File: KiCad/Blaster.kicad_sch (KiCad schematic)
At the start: 32 parts, among them Q1 2N3904, Q2 2N3904, Q3 TIP41, SW2 Fire, SW3 Freq Select, SW4 Fire Select, U2 PIC16F1788-IP, U3 Audio Board

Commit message: Updated blaster schematic
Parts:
- R13: value 40kΩ -> 25kΩ
- R6: value 1kΩ -> 2.2kΩ
- renumbered D5 to D4, D6 to D5
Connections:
- net +5V: no longer D5.1 (K), Q2.3 (C), S1. (-)
- new net: D5.1 (K), Q2.3 (C), S1. (-)
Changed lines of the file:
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@@
 	)
 	(junction
+		(at 237.49 100.33)
+		(diameter 0)
+		(color 0 0 0 0)
+	)
+	(junction
 		(at 33.02 77.47)
 		(diameter 0)
@@
 	)
 	(junction
-		(at 237.49 100.33)
-		(diameter 0)
-		(color 0 0 0 0)
-	)
-	(junction
 		(at 224.79 100.33)
 		(diameter 0)
@@
 	(wire
 		(pts
+			(xy 237.49 99.06) (xy 237.49 100.33)
+		)
+		(stroke
+			(width 0)
+			(type default)
+		)
+	)
+	(wire
+		(pts
 			(xy 57.15 101.6) (xy 52.07 101.6)
 		)
@@
 		(dnp no)
 		(property "Reference" "R13"
-			(at 199.39 113.03 0)
+			(at 199.898 113.03 0)
 			(effects
 				(font
@@
 			)
 		)
-		(property "Value" "40kΩ"
+		(property "Value" "25kΩ"
 			(at 200.914 115.57 0)
 			(effects
@@
 		(dnp no)
 		(fields_autoplaced yes)
-		(property "Reference" "#PWR011"
+		(property "Reference" "#PWR013"
 			(at 81.28 59.69 90)
 			(effects
@@
 			(project "Project"
 				(path "/152b0fc1-fa29-4f64-bd5c-6a59f63b05cf/0b035578-8811-407f-9c52-5736444552f1"
-					(reference "#PWR011")
+					(reference "#PWR013")
 					(unit 1)
 				)
@@
 		(dnp no)
 		(fields_autoplaced yes)
-		(property "Reference" "#PWR010"
+		(property "Reference" "#PWR012"
 			(at 113.03 55.88 90)
 			(effects
@@
 			(project "Project"
 				(path "/152b0fc1-fa29-4f64-bd5c-6a59f63b05cf/0b035578-8811-407f-9c52-5736444552f1"
-					(reference "#PWR010")
+					(reference "#PWR012")
 					(unit 1)
 				)
@@
 		(dnp no)
 		(fields_autoplaced yes)
-		(property "Reference" "#PWR014"
+		(property "Reference" "#PWR016"
 			(at 124.46 115.57 90)
 			(effects
@@
 			(project "Project"
 				(path "/152b0fc1-fa29-4f64-bd5c-6a59f63b05cf/0b035578-8811-407f-9c52-5736444552f1"
-					(reference "#PWR014")
+					(reference "#PWR016")
 					(unit 1)
 				)
@@
 		(dnp no)
 		(fields_autoplaced yes)
-		(property "Reference" "#PWR09"
+		(property "Reference" "#PWR011"
 			(at 52.07 55.88 90)
 			(effects
@@
 			(project "Project"
 				(path "/152b0fc1-fa29-4f64-bd5c-6a59f63b05cf/0b035578-8811-407f-9c52-5736444552f1"
-					(reference "#PWR09")
+					(reference "#PWR011")
 					(unit 1)
 				)
@@
 		(dnp no)
 		(fields_autoplaced yes)
-		(property "Reference" "#PWR016"
+		(property "Reference" "#PWR018"
 			(at 83.82 185.42 90)
 			(effects
@@
 			(project "Project"
 				(path "/152b0fc1-fa29-4f64-bd5c-6a59f63b05cf/0b035578-8811-407f-9c52-5736444552f1"
-					(reference "#PWR016")
+					(reference "#PWR018")
 					(unit 1)
 				)
@@
 		(on_board yes)
 		(dnp no)
-		(property "Reference" "D6"
+		(property "Reference" "D5"
 			(at 226.568 104.394 90)
 			(effects
@@
 			(project "Project"
 				(path "/152b0fc1-fa29-4f64-bd5c-6a59f63b05cf/0b035578-8811-407f-9c52-5736444552f1"
-					(reference "D6")
+					(reference "D5")
 					(unit 1)
 				)
@@
 	)
 	(symbol
-		(lib_id "Libraries:+5V")
-		(at 237.49 99.06 0)
+		(lib_id "AW_Libraries_Power:GND")
+		(at 85.09 102.87 0)
 		(unit 1)
 		(exclude_from_sim no)
@@
 		(dnp no)
 		(fields_autoplaced yes)
-		(property "Reference" "+5V07"
-			(at 237.49 95.25 0)
+		(property "Reference" "#PWR015"
+			(at 81.28 102.87 90)
 			(effects
 				(font
@@
 			)
 		)
-		(property "Value" "+5V"
-			(at 237.49 95.25 0)
+		(property "Value" "GND"
+			(at 81.28 99.06 0)
 			(effects
 				(font
@@
 		)
 		(property "Footprint" ""
-			(at 237.49 95.25 0)
+			(at 85.09 102.87 0)
 			(effects
 				(font
@@
 		)
 		(property "Datasheet" ""
-			(at 237.49 95.25 0)
+			(at 85.09 102.87 0)
 			(effects
 				(font
@@
 		)
 		(property "Description" ""
-			(at 237.49 99.06 0)
+			(at 85.09 102.87 0)
 			(effects
 				(font
@@
 			(project "Project"
 				(path "/152b0fc1-fa29-4f64-bd5c-6a59f63b05cf/0b035578-8811-407f-9c52-5736444552f1"
-					(reference "+5V07")
+					(reference "#PWR015")
 					(unit 1)
 				)
@@
 	)
 	(symbol
-		(lib_id "AW_Libraries_Power:GND")
-		(at 85.09 102.87 0)
+		(lib_id "Libraries:Solenoid")
+		(at 237.49 97.79 0)
 		(unit 1)
 		(exclude_from_sim no)
-		(in_bom no)
-		(on_board no)
+		(in_bom yes)
+		(on_board yes)
 		(dnp no)
 		(fields_autoplaced yes)
-		(property "Reference" "#PWR013"
-			(at 81.28 102.87 90)
+		(property "Reference" "S1"
+			(at 250.19 107.9499 0)
 			(effects
 				(font
 					(size 1.27 1.27)
 				)
-				(hide yes)
+				(justify left)
 			)
 		)
-		(property "Value" "GND"
-			(at 81.28 99.06 0)
+		(property "Value" "Solenoid"
+			(at 250.19 110.4899 0)
 			(effects
 				(font
 					(size 1.27 1.27)
 				)
-				(hide yes)
+				(justify left)
 			)
 		)
-		(property "Footprint" ""
-			(at 85.09 102.87 0)
+		(property "Footprint" "Connector_PinHeader_2.54mm:PinHeader_1x02_P2.54mm_Vertical"
+			(at 239.776 102.87 0)
 			(effects
 				(font
@@
 		)
 		(property "Datasheet" ""
-			(at 85.09 102.87 0)
+			(at 239.776 102.87 0)
 			(effects
 				(font
@@
 		)
 		(property "Description" ""
-			(at 85.09 102.87 0)
+			(at 239.776 102.87 0)
 			(effects
 				(font
@@
 		(pin ""
 		)
+		(pin ""
+		)
 		(instances
 			(project "Project"
 				(path "/152b0fc1-fa29-4f64-bd5c-6a59f63b05cf/0b035578-8811-407f-9c52-5736444552f1"
-					(reference "#PWR013")
+					(reference "S1")
 					(unit 1)
 				)
@@
 	)
 	(symbol
-		(lib_id "Libraries:Solenoid")
-		(at 237.49 97.79 0)
+		(lib_id "Connector:TestPoint")
+		(at 190.5 81.28 0)
 		(unit 1)
 		(exclude_from_sim no)
@@
 		(on_board yes)
 		(dnp no)
-		(fields_autoplaced yes)
-		(property "Reference" "S1"
-			(at 250.19 107.9499 0)
+		(property "Reference" "TP6"
+			(at 188.722 75.692 0)
 			(effects
 				(font
@@
 			)
 		)
-		(property "Value" "Solenoid"
-			(at 250.19 110.4899 0)
+		(property "Value" "TestPoint"
+			(at 193.04 79.2479 0)
 			(effects
 				(font
@@
 				)
 				(justify left)
+				(hide yes)
 			)
 		)
-		(property "Footprint" "Connector_PinHeader_2.54mm:PinHeader_1x02_P2.54mm_Vertical"
-			(at 239.776 102.87 0)
+		(property "Footprint" "AlexWheelockFootprintLibrary:Test Point"
+			(at 195.58 81.28 0)
 			(effects
 				(font
@@
 			)
 		)
-		(property "Datasheet" ""
-			(at 239.776 102.87 0)
+		(property "Datasheet" "~"
+			(at 195.58 81.28 0)
 			(effects
 				(font
@@
 			)
 		)
-		(property "Description" ""
-			(at 239.776 102.87 0)
+		(property "Description" "test point"
+			(at 190.5 81.28 0)
 			(effects
 				(font
@@
 			)
 		)
-		(pin ""
-		)
-		(pin ""
+		(pin "1"
 		)
 		(instances
 			(project "Project"
 				(path "/152b0fc1-fa29-4f64-bd5c-6a59f63b05cf/0b035578-8811-407f-9c52-5736444552f1"
-					(reference "S1")
+					(reference "TP6")
 					(unit 1)
 				)
@@
 	)
 	(symbol
-		(lib_id "Connector:TestPoint")
-		(at 190.5 81.28 0)
+		(lib_id "AW_Libraries_Power:+7.4V")
+		(at 237.49 93.98 0)
 		(unit 1)
 		(exclude_from_sim no)
@@
 		(on_board yes)
 		(dnp no)
-		(property "Reference" "TP6"
-			(at 188.722 75.692 0)
+		(property "Reference" "#PWR19"
+			(at 237.49 93.98 0)
 			(effects
 				(font
 					(size 1.27 1.27)
 				)
-				(justify left)
+				(hide yes)
 			)
 		)
-		(property "Value" "TestPoint"
-			(at 193.04 79.2479 0)
+		(property "Value" "+7.4V"
+			(at 237.49 93.98 0)
 			(effects
 				(font
 					(size 1.27 1.27)
 				)
-				(justify left)
-				(hide yes)
 			)
 		)
-		(property "Footprint" "AlexWheelockFootprintLibrary:Test Point"
-			(at 195.58 81.28 0)
+		(property "Footprint" ""
+			(at 237.49 93.98 0)
 			(effects
 				(font
@@
 			)
 		)
-		(property "Datasheet" "~"
-			(at 195.58 81.28 0)
+		(property "Datasheet" ""
+			(at 237.49 93.98 0)
 			(effects
 				(font
@@
 			)
 		)
-		(property "Description" "test point"
-			(at 190.5 81.28 0)
+		(property "Description" ""
+			(at 237.49 93.98 0)
 			(effects
 				(font
@@
 			)
 		)
-		(pin "1"
+		(pin ""
 		)
 		(instances
 			(project "Project"
 				(path "/152b0fc1-fa29-4f64-bd5c-6a59f63b05cf/0b035578-8811-407f-9c52-5736444552f1"
-					(reference "TP6")
+					(reference "#PWR19")
 					(unit 1)
 				)
@@
 		(dnp no)
 		(fields_autoplaced yes)
-		(property "Reference" "#PWR015"
+		(property "Reference" "#PWR017"
 			(at 220.98 130.81 90)
 			(effects
@@
 			(project "Project"
 				(path "/152b0fc1-fa29-4f64-bd5c-6a59f63b05cf/0b035578-8811-407f-9c52-5736444552f1"
-					(reference "#PWR015")
+					(reference "#PWR017")
 					(unit 1)
 				)
@@
 			)
 		)
-		(property "Value" "1kΩ"
+		(property "Value" "2.2kΩ"
 			(at 199.898 78.74 0)
 			(effects
@@
 		(dnp no)
 		(fields_autoplaced yes)
-		(property "Reference" "#PWR012"
+		(property "Reference" "#PWR014"
 			(at 208.28 87.63 90)
 			(effects
@@
 			(project "Project"
 				(path "/152b0fc1-fa29-4f64-bd5c-6a59f63b05cf/0b035578-8811-407f-9c52-5736444552f1"
-					(reference "#PWR012")
+					(reference "#PWR014")
 					(unit 1)
 				)
@@
 		(dnp no)
 		(fields_autoplaced yes)
-		(property "Reference" "D5"
+		(property "Reference" "D4"
 			(at 83.82 45.72 0)
 			(effects
@@
 			(project "Project"
 				(path "/152b0fc1-fa29-4f64-bd5c-6a59f63b05cf/0b035578-8811-407f-9c52-5736444552f1"
-					(reference "D5")
+					(reference "D4")
 					(unit 1)
 				)

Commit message: Finalized schematics
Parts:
- removed Q1, Q2: 2N3904, Package_TO_SOT_THT:TO-92_Inline, symbol Transistor_BJT:2N3904
- removed Q3: TIP41, Package_TO_SOT_THT:TO-220-3_Vertical, symbol Transistor_BJT:TIP41
- removed SW3: Freq Select, symbol Switch:SW_DIP_x01
- removed TP1, TP2, TP3, TP4, TP5, TP6, TP7: TestPoint, AlexWheelockFootprintLibrary:Test Point, symbol Connector:TestPoint
- added Q1, Q2: BUK9832-55A, Package_TO_SOT_SMD:SOT-223-3_TabPin2, symbol Transistor_FET:BUK7880-55A
- added R15, R7: 0Ω, Resistor_SMD:R_0805_2012Metric_Pad1.20x1.40mm_HandSolder, symbol Libraries:R_Custom
- added SW3: Freq Select, AlexWheelockFootprintLibrary:Project_Blaster_Freq_Switch, symbol Switch:SW_SPDT
- D5: footprint (none) -> Diode_SMD:D_0805_2012Metric_Pad1.15x1.40mm_HandSolder
- LD1, S1: footprint Connector_PinHeader_2.54mm:PinHeader_1x02_P2.54mm_Vertical -> AlexWheelockFootprintLibrary:Project_Locking_Output_Header
- R14: renamed from R13; value 25kΩ -> 100kΩ
- R6: value 2.2kΩ -> 100kΩ
- SW2: footprint (none) -> AlexWheelockFootprintLibrary:Project_Locking_Output_Header
- SW4: footprint (none) -> AlexWheelockFootprintLibrary:Project_Blaster_FireSelect_Switch
- U2: footprint (none) -> AlexWheelockFootprintLibrary:SSOP-28
- U3: footprint (none) -> AlexWheelockFootprintLibrary:Project_Audio_Board
- renumbered R9 to R10, R10 to R11, R11 to R12, R12 to R13, R7 to R8, R8 to R9
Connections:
- net +5V: now also SW3.2 (B)
- net at R14.1: now also U2.14 (RC3/SCK/SCL), Q2.1 (G)
- net at R14.2: no longer U2.14 (RC3/SCK/SCL)
- net at LD1.3 (K): now also Q1.2 (D)
- net at D5.1 (K): now also S1.1 (+); no longer S1. (-)
- net at R6.1: now also U2.13 (RC2/P1A/CCP1), Q1.1 (G)
- net at R13.1: now also S1.2 (-), Q2.2 (D); no longer S1. (-)
- net at R6.2: no longer U2.13 (RC2/P1A/CCP1)
- new net: Q1.3 (S), R7.1
- new net: C8.2, R8.1, SW2.2, U2.21 (INT/AN12/RB0)
- new net: R10.1, SW4.5, U2.23 (P1B/AN8/RB2)
- new net: R9.1, SW3.1 (A), U2.22 (P1C/AN10/RB1)
- new net: Q2.3 (S), R15.1
- no-connect marks 15 -> 16
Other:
- note added: "R8-R12 330Ω"
- note removed: "R7-R11 330Ω"
- moved on the sheet: D5, LD1, R13, R14, R6

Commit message: working on the PCB for the blaster
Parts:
- SW4: footprint AlexWheelockFootprintLibrary:Project_Blaster_FireSelect_Switch -> AlexWheelockFootprintLibrary:Project_Locking_Header_1x06
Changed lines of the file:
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@@
 			)
 		)
-		(property "Footprint" "AlexWheelockFootprintLibrary:Project_Blaster_FireSelect_Switch"
+		(property "Footprint" "AlexWheelockFootprintLibrary:Project_Locking_Header_1x06"
 			(at 44.45 96.52 0)
 			(effects

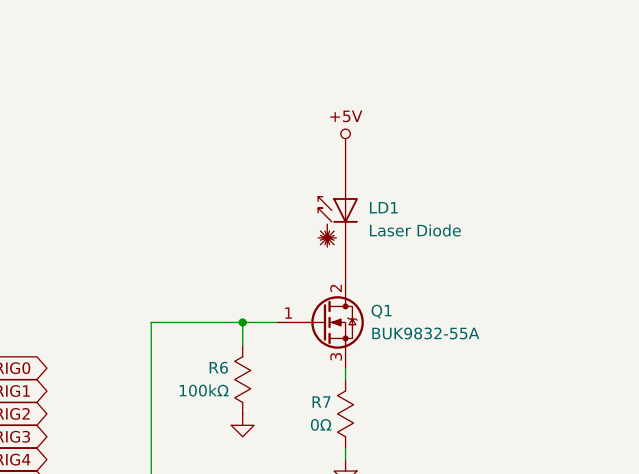
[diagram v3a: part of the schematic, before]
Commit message: got a lot done on the blaster PCB
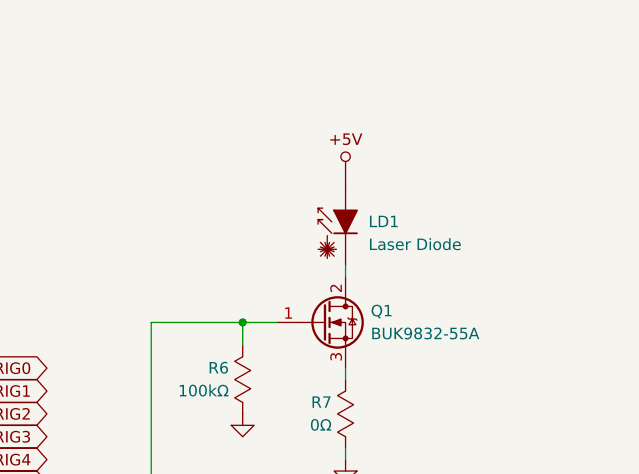
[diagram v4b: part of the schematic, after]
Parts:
- LD1: symbol Device:D_Laser_1A3C -> Libraries:Laser_Diode
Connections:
- net at Q1.2 (D): now also LD1.2 (K); no longer LD1.3 (K)
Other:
- moved on the sheet: LD1
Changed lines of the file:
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@@
 	(wire
 		(pts
+			(xy 205.74 53.34) (xy 205.74 54.61)
+		)
+		(stroke
+			(width 0)
+			(type default)
+		)
+	)
+	(wire
+		(pts
 			(xy 198.12 100.33) (xy 198.12 102.87)
 		)
@@
 	)
 	(symbol
-		(lib_id "Device:D_Laser_1A3C")
-		(at 205.74 46.99 90)
+		(lib_id "Libraries:Laser_Diode")
+		(at 198.12 48.26 90)
 		(unit 1)
 		(exclude_from_sim no)
@@
 		(fields_autoplaced yes)
 		(property "Reference" "LD1"
-			(at 208.28 46.9899 90)
+			(at 208.28 48.5139 90)
 			(effects
 				(font
@@
 		)
 		(property "Value" "Laser Diode"
-			(at 208.28 49.5299 90)
+			(at 208.28 51.0539 90)
 			(effects
 				(font
@@
 		)
 		(property "Footprint" "AlexWheelockFootprintLibrary:Project_Locking_Output_Header"
-			(at 206.375 49.53 0)
+			(at 198.12 48.26 0)
 			(effects
 				(font
@@
 		)
 		(property "Datasheet" "~"
-			(at 210.82 46.228 0)
+			(at 198.12 48.26 0)
 			(effects
 				(font
@@
 		)
 		(property "Description" "Laser diode, cathode on pin 3, anode on pin 1"
-			(at 205.74 46.99 0)
+			(at 198.12 48.26 0)
 			(effects
 				(font
@@
 		(pin "1"
 		)
-		(pin "3"
+		(pin "2"
 		)
 		(instances
@@
 	(symbol
 		(lib_id "Libraries:+5V")
-		(at 205.74 40.64 0)
+		(at 205.74 43.18 0)
 		(unit 1)
 		(exclude_from_sim no)
@@
 		(fields_autoplaced yes)
 		(property "Reference" "#+5V03"
-			(at 205.74 36.83 0)
+			(at 205.74 39.37 0)
 			(effects
 				(font
@@
 		)
 		(property "Value" "+5V"
-			(at 205.74 36.83 0)
+			(at 205.74 39.37 0)
 			(effects
 				(font
@@
 		)
 		(property "Footprint" ""
-			(at 205.74 36.83 0)
+			(at 205.74 39.37 0)
 			(effects
 				(font
@@
 		)
 		(property "Datasheet" ""
-			(at 205.74 36.83 0)
+			(at 205.74 39.37 0)
 			(effects
 				(font
@@
 		)
 		(property "Description" ""
-			(at 205.74 40.64 0)
+			(at 205.74 43.18 0)
 			(effects
 				(font

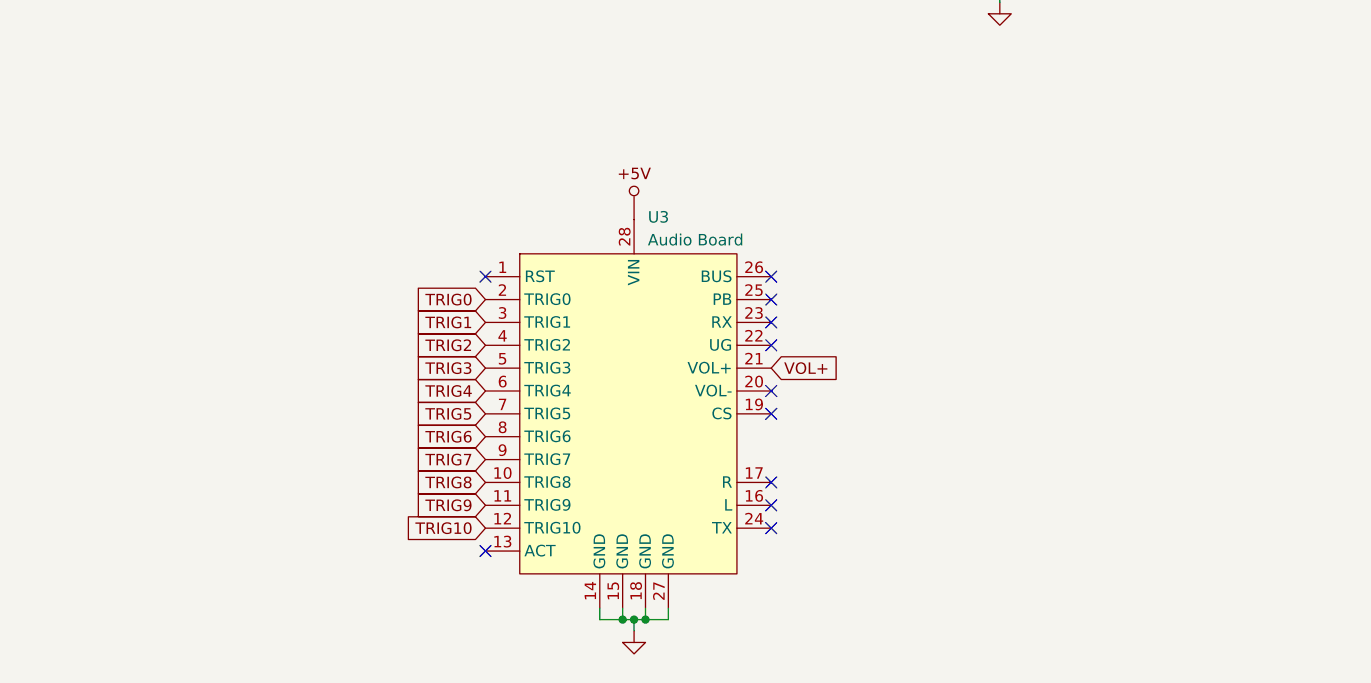
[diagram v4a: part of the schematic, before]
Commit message: added title block and logo
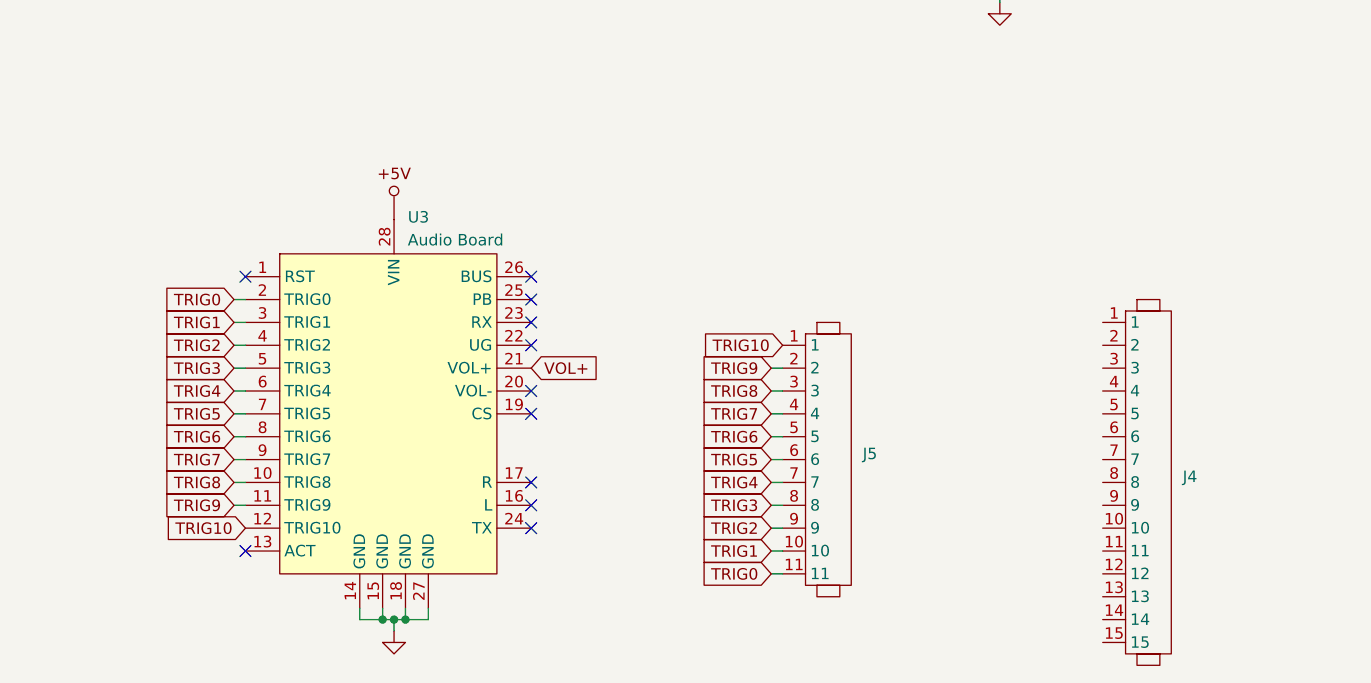
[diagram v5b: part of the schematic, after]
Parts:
- added J4: ~, symbol Libraries:Header_1x15
- added J5: ~, symbol Libraries:Header_1x11
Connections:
- net TRIG0: now also J5.11
- net TRIG1: now also J5.10
- net TRIG10: now also J5.1
- net TRIG2: now also J5.9
- net TRIG3: now also J5.8
- net TRIG4: now also J5.7
- net TRIG5: now also J5.6
- net TRIG6: now also J5.5
- net TRIG7: now also J5.4
- net TRIG8: now also J5.3
- net TRIG9: now also J5.2
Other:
- moved on the sheet: U3
